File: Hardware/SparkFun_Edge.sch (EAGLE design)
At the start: 64 parts, among them J5 CORTEX_DEBUG, J7 CAMERA-HIMAX, U2 LIS2DH12, U3 1.8V, U5 ARTEMIS_MODULESMD, Y2 32.768kHz

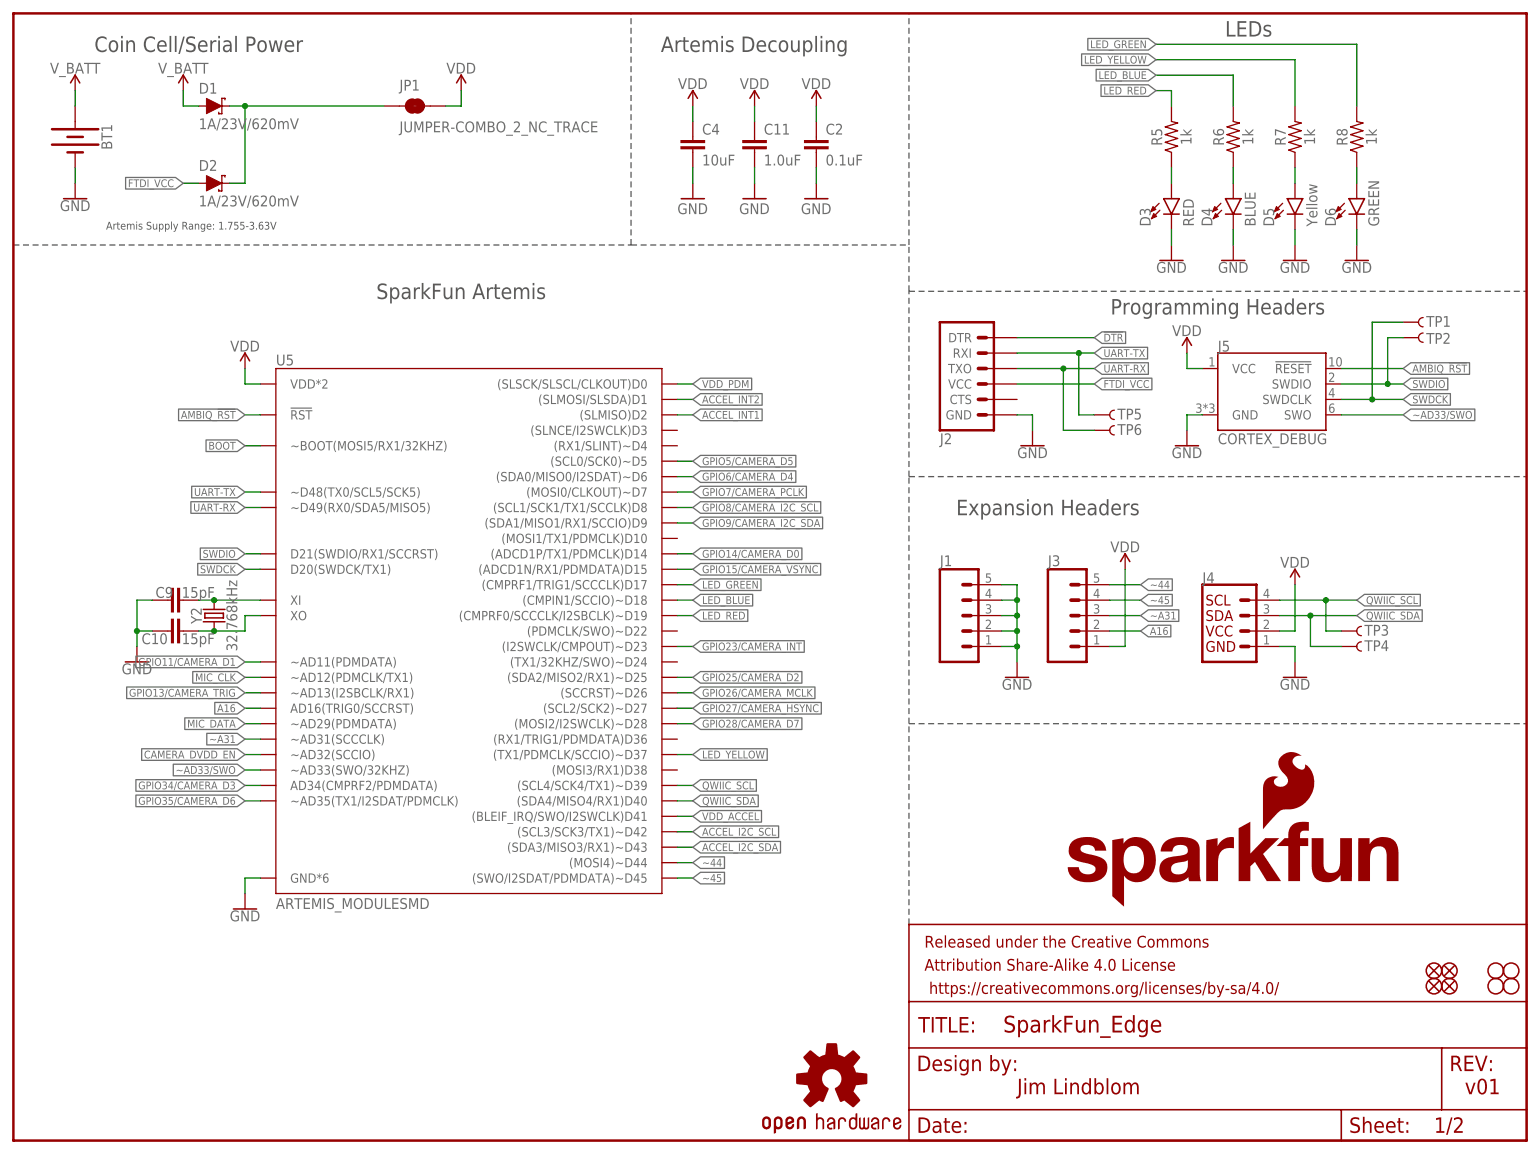
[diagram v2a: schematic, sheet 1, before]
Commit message: re-assign camera pins for fast gpio compatibility
Camera Pin : FAST GPIO Bit : Apollo3 Pad
D0 : D0 : 24
D1 : D1 : 33
D2 : D2 : 10
D3 : D3 : 11
D4 : D4 : 28
D5 : D5 : 5
D6 : D6 : 14
D7 : D7 : 23
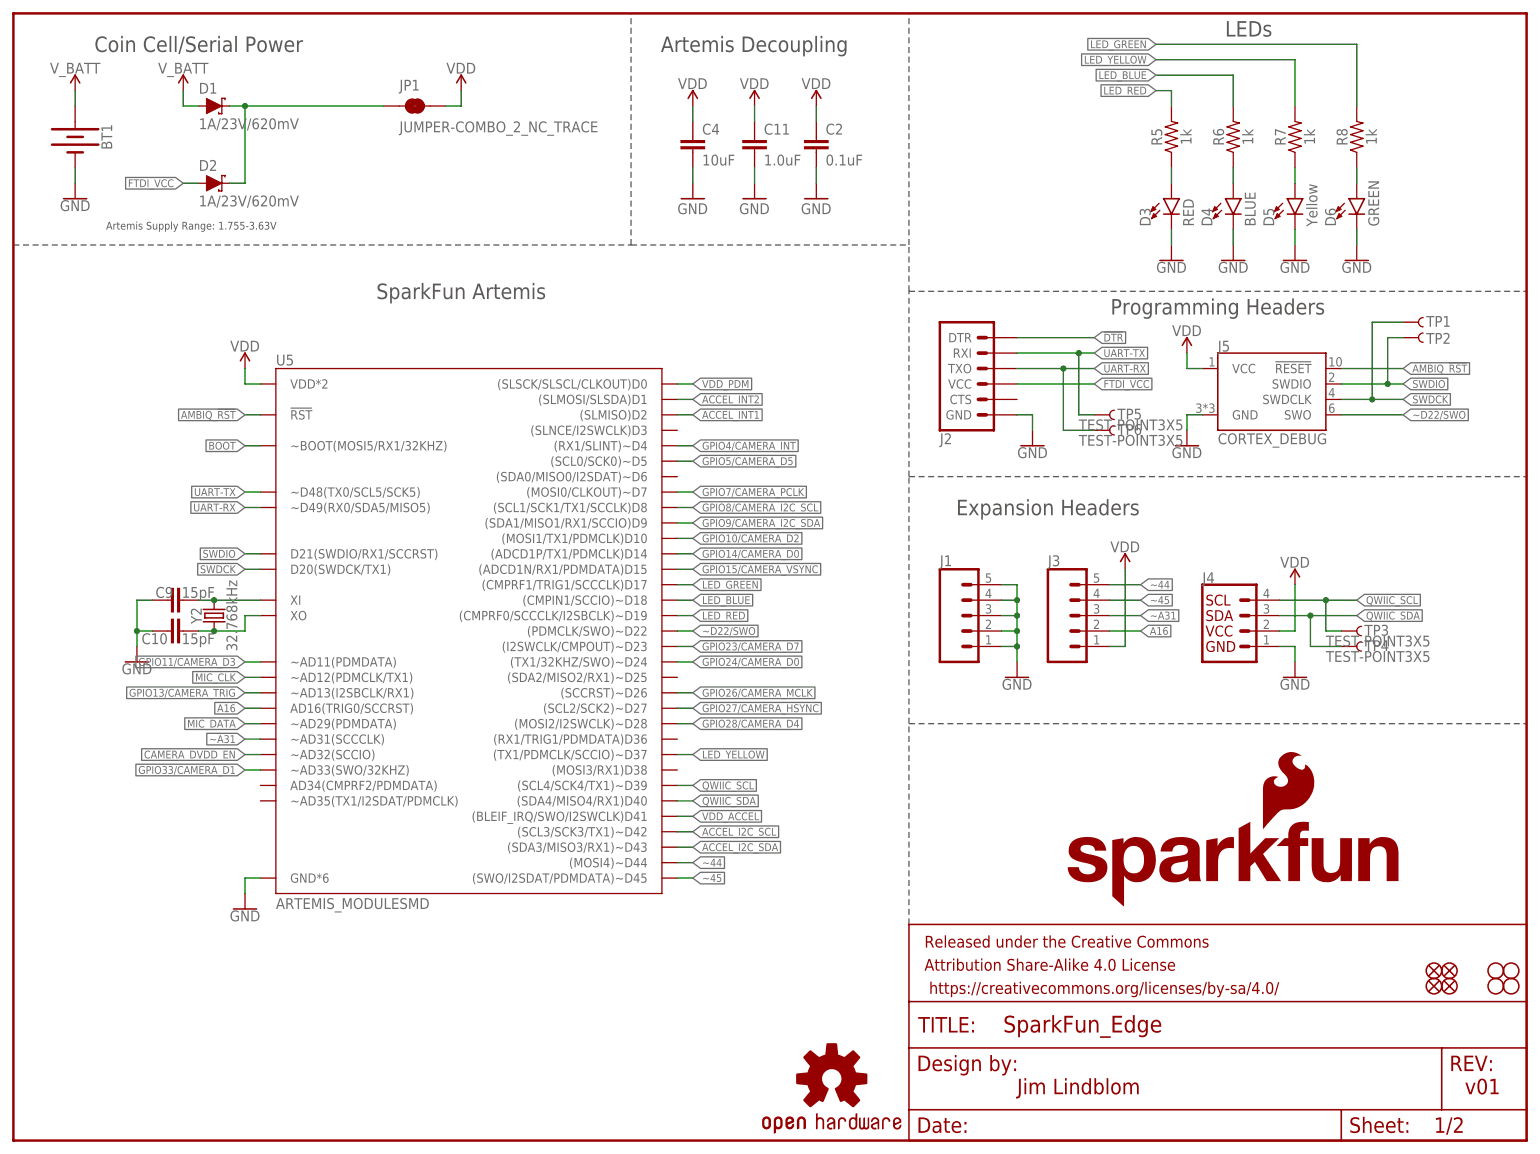
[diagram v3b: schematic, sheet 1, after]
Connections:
- removed net GPIO11/CAMERA_D1: J7.D1, U5.~AD11(PDMDATA)
- removed net GPIO23/CAMERA_INT: J7.INT, U5.(I2SWCLK/CMPOUT)~D23
- removed net GPIO25/CAMERA_D2: J7.D2, U5.(SDA2/MISO2/RX1)~D25
- removed net GPIO28/CAMERA_D7: J7.D7, U5.(MOSI2/I2SWCLK)~D28
- removed net GPIO34/CAMERA_D3: J7.D3, U5.AD34(CMPRF2/PDMDATA)
- removed net GPIO35/CAMERA_D6: J7.D6, U5.~AD35(TX1/I2SDAT/PDMCLK)
- removed net GPIO6/CAMERA_D4: J7.D4, U5.(SDA0/MISO0/I2SDAT)~D6
- removed net ~AD33/SWO: J5.SWO, U5.~AD33(SWO/32KHZ)
- new net GPIO10/CAMERA_D2: J7.D2, U5.(MOSI1/TX1/PDMCLK)D10
- new net GPIO11/CAMERA_D3: J7.D3, U5.~AD11(PDMDATA)
- new net GPIO23/CAMERA_D7: J7.D7, U5.(I2SWCLK/CMPOUT)~D23
- new net GPIO24/CAMERA_D0: J7.D0, U5.(TX1/32KHZ/SWO)~D24
- new net GPIO28/CAMERA_D4: J7.D4, U5.(MOSI2/I2SWCLK)~D28
- new net GPIO33/CAMERA_D1: J7.D1, U5.~AD33(SWO/32KHZ)
- new net GPIO4/CAMERA_INT: J7.INT, U5.(RX1/SLINT)~D4
- new net ~D22/SWO: J5.SWO, U5.(PDMCLK/SWO)~D22
- net GPIO14/CAMERA_D0: now also J7.D6; no longer J7.D0
